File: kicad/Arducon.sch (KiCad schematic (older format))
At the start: 59 parts, among them J101 To Radio, J102 DB9 Female, J103 To Antenna, J104 Conn_01x08, J105 Conn_01x08, J106 Logic Level, J107 Conn_01x02, J108 Controlled Device Power, J109 Conn_01x01, J110 Conn_01x01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

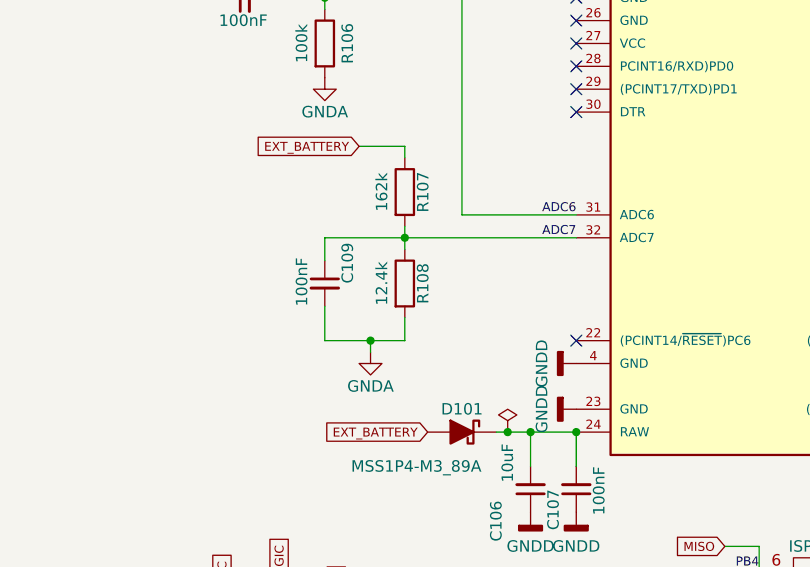
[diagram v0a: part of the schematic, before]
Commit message: Changed R108 to 10k
Changed R108 to a more common resistor value.
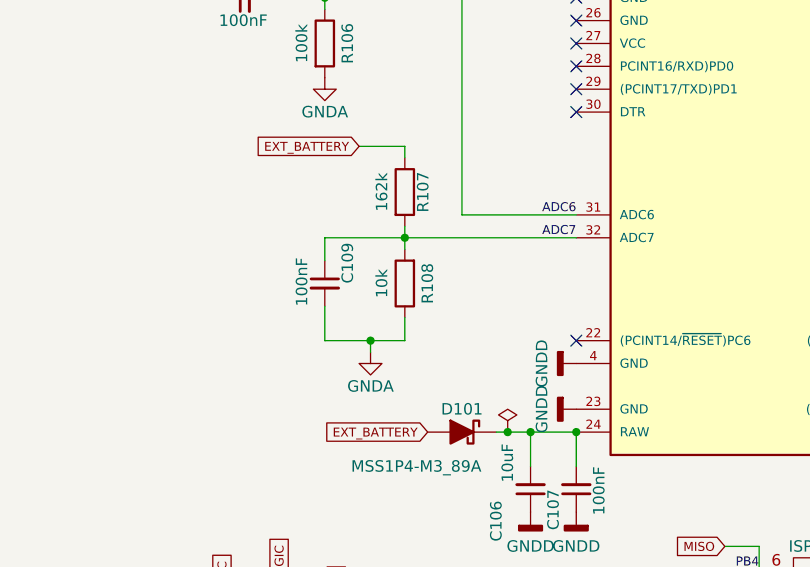
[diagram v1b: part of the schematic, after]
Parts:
- R108: value 12.4k -> 10k; Link <a href=\"https://www.digikey.com/products/en?keywords=P12.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 -> <a href=\"https://www.digikey.com/products/en?keywords=311-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; Part No. P12.4KCCT-ND -> 311-10.0KCRCT-ND
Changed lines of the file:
@@
-$EndComp
-$Comp
-L Device:R R108
-U 1 1 5F9E5C35
-P 3450 6450
-F 0 "R108" V 3530 6450 50  0000 C CNN
-F 1 "12.4k" V 3350 6450 50  0000 C CNN
-F 2 "Resistors_SMD:R_0805" V 3380 6450 50  0001 C CNN
-F 3 "" H 3450 6450 50  0001 C CNN
-F 4 "P12.4KCCT-ND" H 3450 6450 50  0001 C CNN "Part No."
-F 5 "<a href=\"https://www.digikey.com/products/en?keywords=P12.4KCCT-ND\">Link</a>" H 3450 6450 50  0001 C CNN "Link"
-	1    3450 6450
-	1    0    0    -1
 $EndComp
 $Comp
@@
 	0    1    1    0
 $EndComp
+$Comp
+L Device:R R108
+U 1 1 5FE52722
+P 3450 6450
+F 0 "R108" V 3350 6450 50  0000 C CNN
+F 1 "10k" V 3550 6450 50  0000 C CNN
+F 2 "Resistors_SMD:R_0805" H 3380 6450 50  0001 C CNN
+F 3 "" H 3450 6450 50  0001 C CNN
+F 4 "311-10.0KCRCT-ND" H 3450 6450 60  0001 C CNN "Part No."
+F 5 "<a href=\"https://www.digikey.com/products/en?keywords=311-10.0KCRCT-ND\">Link</a>" H 3450 6450 60  0001 C CNN "Link"
+	1    3450 6450
+	-1   0    0    1
+$EndComp
 Wire Bus Line

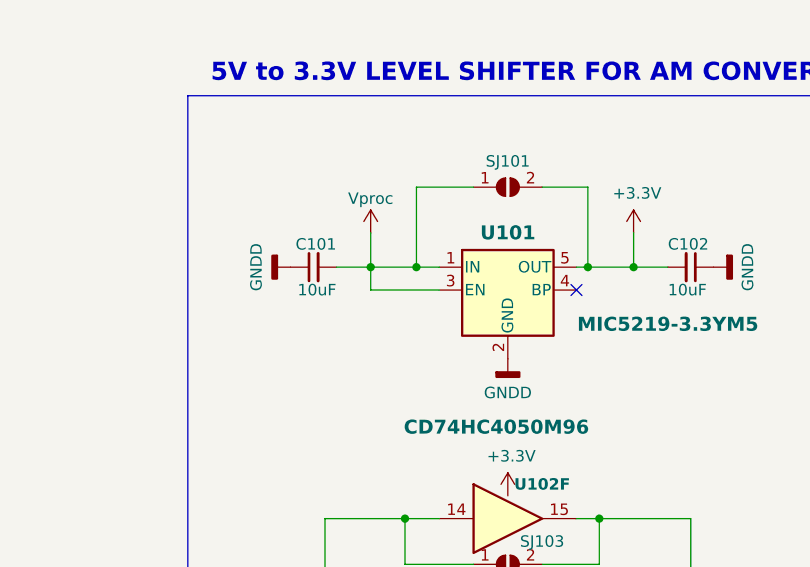
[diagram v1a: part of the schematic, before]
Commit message: Q102 Footprint
Corrected Q102 footprint - it required an SOT363 with a pitch of 0.65mm instead of 0.50
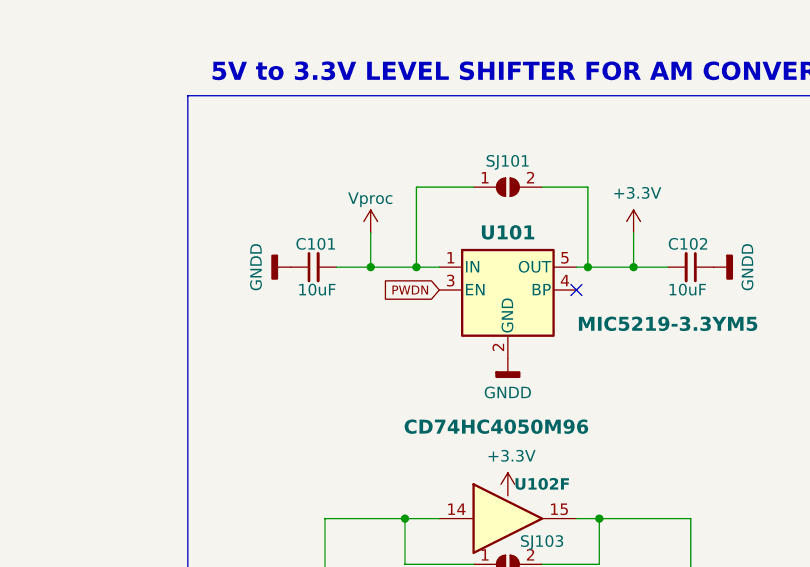
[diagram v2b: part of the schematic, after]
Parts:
- Q102: footprint TO_SOT_Packages_SMD:SOT-363 -> TO_SOT_Packages_SMD:SOT-363-0.65
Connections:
- wire segments 254 -> 252
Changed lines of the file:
@@
 Wire Wire Line
 	9750 1600 9600 1600
-Wire Wire Line
-	10050 1700 9750 1700
-Wire Wire Line
-	9750 1700 9750 1600
 NoConn ~ 10650 1700
 $Comp
@@
 F 0 "Q102" H 13700 8300 61  0000 C CNB
 F 1 "LMN400E01" H 13700 8192 61  0000 C CNB
-F 2 "TO_SOT_Packages_SMD:SOT-363" H 13715 7500 50  0001 L CNN
+F 2 "TO_SOT_Packages_SMD:SOT-363-0.65" H 13715 7500 50  0001 L CNN
 F 3 "" H 13715 7500 50  0001 L CNN
 F 4 "LMN400E01DICT-ND" H 13700 7700 50  0001 C CNN "Part No."
@@
 	-1   0    0    1
 $EndComp
+Text GLabel 10050 1700 0    39   Input ~ 0
+PWDN
 Wire Bus Line
 	6300 4600 6300 7300

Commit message: Schematic Cleanup
o Cleaned up some schematic confusion
o Routed PWDN to enable on U101
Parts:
- J107: value Conn_01x02 -> External Power Source
- J108: value Controlled Device Power -> Controlled Power
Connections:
- net labels removed: EXT_BATTERY+, GND
- wire segments 252 -> 253
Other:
- note added: "5V to 3.3V LEVEL SHIFTER FOR AM MODULATOR"
- note added: "AM MODULATOR BOARD"
- note removed: "5V to 3.3V LEVEL SHIFTER FOR AM CONVERTER"
- note removed: "CW/FM to AM CONVERTER BOARD"
- moved on the sheet: J107, J108, Q102
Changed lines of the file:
@@
-$EndComp
-$Comp
-L power:GND #PWR0146
-U 1 1 59203AA4
-P 11350 10300
-F 0 "#PWR0146" H 11350 10050 50  0001 C CNN
-F 1 "GND" H 11350 10150 50  0000 C CNN
-F 2 "" H 11350 10300 50  0000 C CNN
-F 3 "" H 11350 10300 50  0000 C CNN
-	1    11350 10300
-	1    0    0    -1
 $EndComp
 $Comp
@@
 	6400 6800 7000 6800
 Wire Wire Line
-	11350 10300 11350 10200
-Wire Wire Line
 	11550 9750 11550 9850
 Wire Wire Line
@@
 Text GLabel 6550 7000 2    39   Output ~ 0
 PWDN
-Text GLabel 14900 7250 0    39   Output ~ 0
-EXT_BATTERY+
 Text GLabel 1800 4250 2    39   Input ~ 0
 TONE_LOGIC
@@
 Text GLabel 1800 4450 2    39   Input ~ 0
 PTT_LOGIC
-Text GLabel 14900 7150 0    39   Output ~ 0
+Text GLabel 14750 8100 0    39   Output ~ 0
 EXT_PWR_GROUND
 $Comp
@@
 Text GLabel 3250 5850 0    39   Input ~ 0
 EXT_BATTERY
-Wire Wire Line
-	11350 10200 11550 10200
 $Comp
 L Device:R R107
@@
 L Arducon-rescue:LMN200B01-Two-band-Tx Q102
 U 1 1 5FC59E4B
-P 13700 7700
-F 0 "Q102" H 13700 8300 61  0000 C CNB
-F 1 "LMN400E01" H 13700 8192 61  0000 C CNB
-F 2 "TO_SOT_Packages_SMD:SOT-363-0.65" H 13715 7500 50  0001 L CNN
-F 3 "" H 13715 7500 50  0001 L CNN
-F 4 "LMN400E01DICT-ND" H 13700 7700 50  0001 C CNN "Part No."
-F 5 "<a href=\"https://www.digikey.com/products/en?keywords=LMN400E01DICT-ND\">Link</a>" H 13700 7700 50  0001 C CNN "Link"
-	1    13700 7700
-	1    0    0    -1
-$EndComp
-Text GLabel 13450 7500 0    39   Input ~ 0
+P 13550 7600
+F 0 "Q102" H 13550 8200 61  0000 C CNB
+F 1 "LMN400E01" H 13550 8092 61  0000 C CNB
+F 2 "TO_SOT_Packages_SMD:SOT-363-0.65" H 13565 7400 50  0001 L CNN
+F 3 "" H 13565 7400 50  0001 L CNN
+F 4 "LMN400E01DICT-ND" H 13550 7600 50  0001 C CNN "Part No."
+F 5 "<a href=\"https://www.digikey.com/products/en?keywords=LMN400E01DICT-ND\">Link</a>" H 13550 7600 50  0001 C CNN "Link"
+	1    13550 7600
+	1    0    0    -1
+$EndComp
+Text GLabel 13300 7400 0    39   Input ~ 0
 PWDN
 $Comp
 L power:GNDD #PWR0141
 U 1 1 5FC5EC97
-P 13950 7600
-F 0 "#PWR0141" H 13950 7350 50  0001 C CNN
-F 1 "GNDD" H 13950 7450 50  0000 C CNN
-F 2 "" H 13950 7600 50  0000 C CNN
-F 3 "" H 13950 7600 50  0000 C CNN
-	1    13950 7600
+P 13800 7500
+F 0 "#PWR0141" H 13800 7250 50  0001 C CNN
+F 1 "GNDD" H 13800 7350 50  0000 C CNN
+F 2 "" H 13800 7500 50  0000 C CNN
+F 3 "" H 13800 7500 50  0000 C CNN
+	1    13800 7500
 	0    -1   -1   0
 $EndComp
 Wire Wire Line
-	13950 7350 14050 7350
-Wire Wire Line
-	14050 7350 14050 6950
-Wire Wire Line
-	14050 6950 13050 6950
-Wire Wire Line
-	13050 6950 13050 7900
-Wire Wire Line
-	13050 7900 13450 7900
-Wire Wire Line
-	13950 7800 14350 7800
+	13800 7250 13900 7250
+Wire Wire Line
+	13900 7250 13900 6850
+Wire Wire Line
+	13900 6850 12900 6850
+Wire Wire Line
+	12900 6850 12900 7800
+Wire Wire Line
+	12900 7800 13300 7800
+Wire Wire Line
+	13800 7700 14200 7700
 Wire Bus Line
 	12100 6700 12100 8250
-Wire Bus Line
-	12100 8250 16200 8250
 Wire Bus Line
 	16200 8250 16200 6700
@@
 Text Notes 13150 6650 0    79   ~ 16
 OPTIONAL EXTERNAL POWER CONTROL
-Text GLabel 13950 8050 2    39   Input ~ 0
-EXT_BATTERY+
 $Comp
 L Connector_Generic:Conn_01x02 J108
 U 1 1 5FCE82B0
-P 15100 7900
-F 0 "J108" H 15180 7892 50  0000 L CNN
-F 1 "Controlled Device Power" H 15100 8000 50  0000 L CNN
-F 2 "Wire_Pads:SolderWirePad_2x_1-5mmDrill_Polarized" H 15100 7900 50  0001 C CNN
-F 3 "" H 15100 7900 50  0001 C CNN
-F 4 "np" H 15100 7900 50  0001 C CNN "Part No."
-F 5 "np" H 15100 7900 50  0001 C CNN "Link"
-	1    15100 7900
+P 14950 7800
+F 0 "J108" H 15030 7792 50  0000 L CNN
+F 1 "Controlled Power" H 15100 7700 50  0000 L CNN
+F 2 "Wire_Pads:SolderWirePad_2x_1-5mmDrill_Polarized" H 14950 7800 50  0001 C CNN
+F 3 "" H 14950 7800 50  0001 C CNN
+F 4 "np" H 14950 7800 50  0001 C CNN "Part No."
+F 5 "np" H 14950 7800 50  0001 C CNN "Link"
+	1    14950 7800
 	1    0    0    1
 $EndComp
@@
 Wire Wire Line
 	14050 3750 14050 3650
-Text Notes 13200 800  0    79   ~ 16
-CW/FM to AM CONVERTER BOARD
+Text Notes 13450 800  0    79   ~ 16
+AM MODULATOR BOARD
 Wire Bus Line
 	8950 850  11950 850
@@
 	8950 6000 8950 850
 Text Notes 9050 800  0    79   ~ 16
-5V to 3.3V LEVEL SHIFTER FOR AM CONVERTER
+5V to 3.3V LEVEL SHIFTER FOR AM MODULATOR
 Wire Wire Line
 	11450 4600 12600 4600
@@
 Connection ~ 11450 3900
 Connection ~ 12600 3900
-Text GLabel 14400 7600 2    39   Output ~ 0
+Text GLabel 14250 7500 2    39   Output ~ 0
 Controlled_Power
 Wire Wire Line
-	14400 7600 14350 7600
-Wire Wire Line
-	14350 7600 14350 7800
-Wire Wire Line
-	14350 7800 14900 7800
+	14250 7500 14200 7500
+Wire Wire Line
+	14200 7500 14200 7700
+Wire Wire Line
+	14200 7700 14750 7700
 Text GLabel 1800 2900 2    39   Input ~ 0
 Controlled_Power
@@
 Text GLabel 1800 3400 2    39   Input ~ 0
 TXD
-Text GLabel 14900 7900 0    39   Input ~ 0
+Text GLabel 14750 7800 0    39   Input ~ 0
 EXT_PWR_GROUND
-Connection ~ 14350 7800
+Connection ~ 14200 7700
 $Comp
 L Connector_Generic:Conn_01x02 J107
 U 1 1 5FE800D7
-P 15100 7150
-F 0 "J107" H 15180 7142 50  0000 L CNN
-F 1 "Conn_01x02" H 15180 7051 50  0000 L CNN
-F 2 "Wire_Pads:SolderWirePad_2x_1-5mmDrill_Polarized" H 15100 7150 50  0001 C CNN
-F 3 "" H 15100 7150 50  0001 C CNN
-F 4 "np" H 15100 7150 50  0001 C CNN "Part No."
-F 5 "np" H 15100 7150 50  0001 C CNN "Link"
-	1    15100 7150
-	1    0    0    -1
+P 14950 8100
+F 0 "J107" H 15030 8092 50  0000 L CNN
+F 1 "External Power Source" H 15100 8000 50  0000 L CNN
+F 2 "Wire_Pads:SolderWirePad_2x_1-5mmDrill_Polarized" H 14950 8100 50  0001 C CNN
+F 3 "" H 14950 8100 50  0001 C CNN
+F 4 "np" H 14950 8100 50  0001 C CNN "Part No."
+F 5 "np" H 14950 8100 50  0001 C CNN "Link"
+	1    14950 8100
+	1    0    0    1
 $EndComp
 $Comp
@@
 PWDN
 Wire Bus Line
+	12100 8250 16200 8250
+Wire Wire Line
+	13800 7950 14450 7950
+Wire Wire Line
+	14450 7950 14450 8000
+Wire Wire Line
+	14450 8000 14750 8000
+Wire Bus Line
 	6300 4600 6300 7300
